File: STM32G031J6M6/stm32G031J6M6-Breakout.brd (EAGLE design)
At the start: 29.1 x 48.3 mm, 22 parts, among them IC1 LDL112D33R, J2 PWR

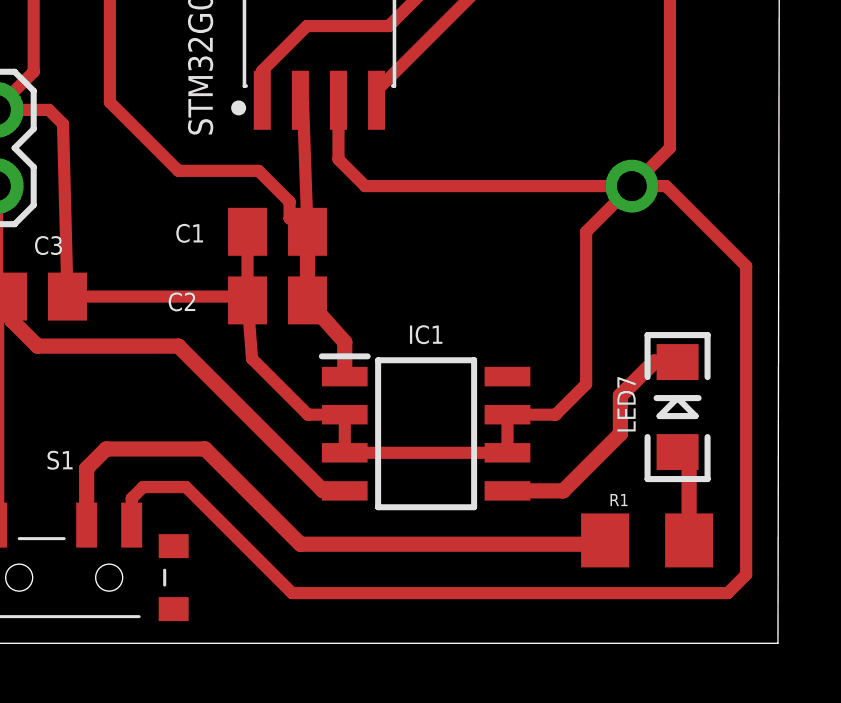
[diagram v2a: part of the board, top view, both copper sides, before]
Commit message: adding rgb breakout
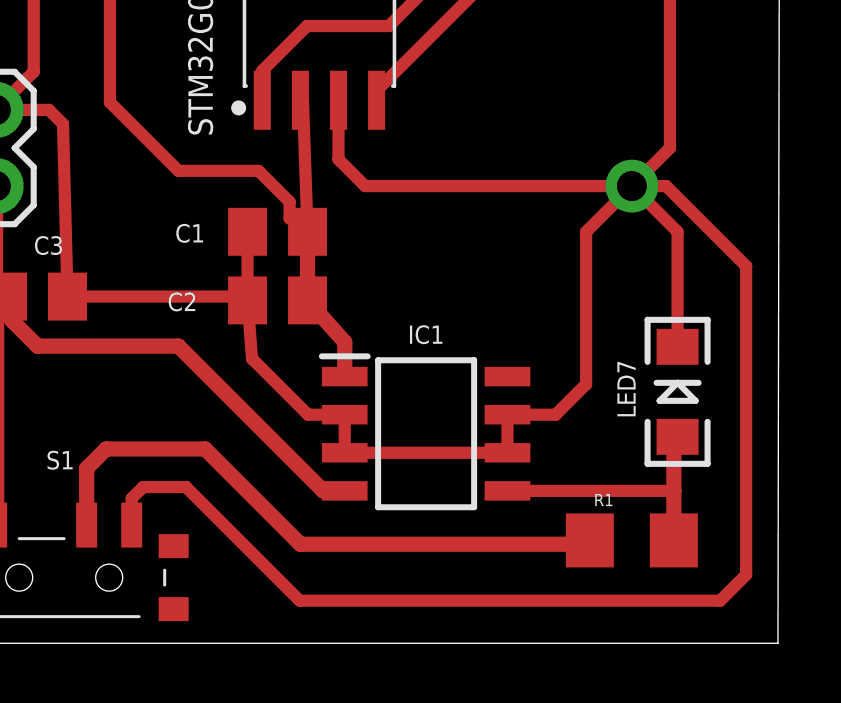
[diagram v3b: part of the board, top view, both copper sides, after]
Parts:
- moved R1 0.51 mm to (24.1, 3.43)
- moved LED7 0.51 mm to (25.7, 8.38)
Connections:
- removed net N$16: IC1.5, LED7.C
- net GND: now also LED7.C
- net N$14: now also IC1.5
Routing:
- net N$16: track 8.19 -> 0.00 mm
- net GND: track 182.5 -> 188.7 mm
- net N$14: track 3.10 -> 9.05 mm
- net EN: track 20.8 -> 20.3 mm
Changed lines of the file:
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@@
 <attribute name="VALUE" x="11.049" y="40.386" size="0.4064" layer="27" rot="R90"/>
 </element>
-<element name="LED7" library="leds" package="LED-1206" value="" x="25.654" y="7.874" smashed="yes" rot="R90">
-<attribute name="NAME" x="24.257" y="6.985" size="0.6096" layer="25" rot="R90"/>
-<attribute name="VALUE" x="27.432" y="6.858" size="0.4064" layer="27" rot="R90"/>
-</element>
-<element name="R1" library="passives" package="1206" value="56 R" x="24.638" y="3.429" smashed="yes">
-<attribute name="NAME" x="23.368" y="4.572" size="0.4064" layer="25"/>
-<attribute name="VALUE" x="23.241" y="1.905" size="0.4064" layer="27"/>
+<element name="LED7" library="leds" package="LED-1206" value="" x="25.654" y="8.382" smashed="yes" rot="R90">
+<attribute name="NAME" x="24.257" y="7.493" size="0.6096" layer="25" rot="R90"/>
+<attribute name="VALUE" x="27.432" y="7.366" size="0.4064" layer="27" rot="R90"/>
+</element>
+<element name="R1" library="passives" package="1206" value="56 R" x="24.13" y="3.429" smashed="yes">
+<attribute name="NAME" x="22.86" y="4.572" size="0.4064" layer="25"/>
+<attribute name="VALUE" x="22.733" y="1.905" size="0.4064" layer="27"/>
 </element>
 <element name="R2" library="passives" package="1206" value="56 R" x="21.971" y="35.433" smashed="yes" rot="R270">
@@
 <wire x1="7.457" y1="3.939" x2="7.457" y2="4.828" width="0.4064" layer="1"/>
 <wire x1="7.836" y1="5.207" x2="7.457" y2="4.828" width="0.4064" layer="1"/>
-<wire x1="12.80498125" y1="1.67301875" x2="27.32701875" y2="1.67301875" width="0.4064" layer="1"/>
-<wire x1="27.32701875" y1="1.67301875" x2="27.94" y2="2.286" width="0.4064" layer="1"/>
+<wire x1="13.05898125" y1="1.41901875" x2="27.07301875" y2="1.41901875" width="0.4064" layer="1"/>
+<wire x1="27.07301875" y1="1.41901875" x2="27.94" y2="2.286" width="0.4064" layer="1"/>
 <wire x1="7.836" y1="5.207" x2="9.271" y2="5.207" width="0.4064" layer="1"/>
-<wire x1="9.271" y1="5.207" x2="12.80498125" y2="1.67301875" width="0.4064" layer="1"/>
+<wire x1="9.271" y1="5.207" x2="13.05898125" y2="1.41901875" width="0.4064" layer="1"/>
 <wire x1="14.351" y1="18.1006" x2="14.351" y2="16.129" width="0.4064" layer="1"/>
 <wire x1="14.351" y1="16.129" x2="15.24" y2="15.24" width="0.4064" layer="1"/>
@@
 <via x="24.13" y="15.24" extent="1-16" drill="1"/>
 <wire x1="24.13" y1="15.24" x2="25.4" y2="16.51" width="0.4064" layer="1"/>
+<contactref element="LED7" pad="C"/>
+<wire x1="25.654" y1="9.882" x2="25.654" y2="13.716" width="0.4064" layer="1"/>
+<wire x1="25.654" y1="13.716" x2="24.13" y2="15.24" width="0.4064" layer="1"/>
 </signal>
 <signal name="VIN">
@@
 <wire x1="6.604" y1="6.477" x2="9.906" y2="6.477" width="0.508" layer="1"/>
 <wire x1="9.906" y1="6.477" x2="13.081" y2="3.302" width="0.508" layer="1"/>
-<wire x1="23.238" y1="3.429" x2="23.111" y2="3.302" width="0.508" layer="1"/>
-<wire x1="23.111" y1="3.302" x2="13.081" y2="3.302" width="0.508" layer="1"/>
+<wire x1="22.73" y1="3.429" x2="22.603" y2="3.302" width="0.508" layer="1"/>
+<wire x1="22.603" y1="3.302" x2="13.081" y2="3.302" width="0.508" layer="1"/>
 </signal>
 <signal name="N$2">
@@
 <contactref element="R1" pad="2"/>
 <contactref element="LED7" pad="A"/>
-<wire x1="26.038" y1="3.429" x2="26.038" y2="5.99" width="0.508" layer="1"/>
-<wire x1="26.038" y1="5.99" x2="25.654" y2="6.374" width="0.508" layer="1"/>
-</signal>
-<signal name="N$16">
-<contactref element="LED7" pad="C"/>
+<wire x1="25.654" y1="6.882" x2="25.53" y2="6.758" width="0.508" layer="1"/>
+<wire x1="25.53" y1="6.758" x2="25.53" y2="5.08" width="0.508" layer="1"/>
 <contactref element="IC1" pad="5"/>
-<wire x1="19.984" y1="5.08" x2="21.844" y2="5.08" width="0.508" layer="1"/>
-<wire x1="21.844" y1="5.08" x2="23.749" y2="6.985" width="0.508" layer="1"/>
-<wire x1="23.749" y1="6.985" x2="23.749" y2="8.255" width="0.508" layer="1"/>
-<wire x1="23.749" y1="8.255" x2="24.868" y2="9.374" width="0.508" layer="1"/>
-<wire x1="24.868" y1="9.374" x2="25.654" y2="9.374" width="0.508" layer="1"/>
+<wire x1="25.53" y1="5.08" x2="25.53" y2="3.429" width="0.508" layer="1"/>
+<wire x1="19.984" y1="5.08" x2="25.53" y2="5.08" width="0.4064" layer="1"/>
 </signal>
 </signals>
